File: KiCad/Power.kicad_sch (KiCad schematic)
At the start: 17 parts

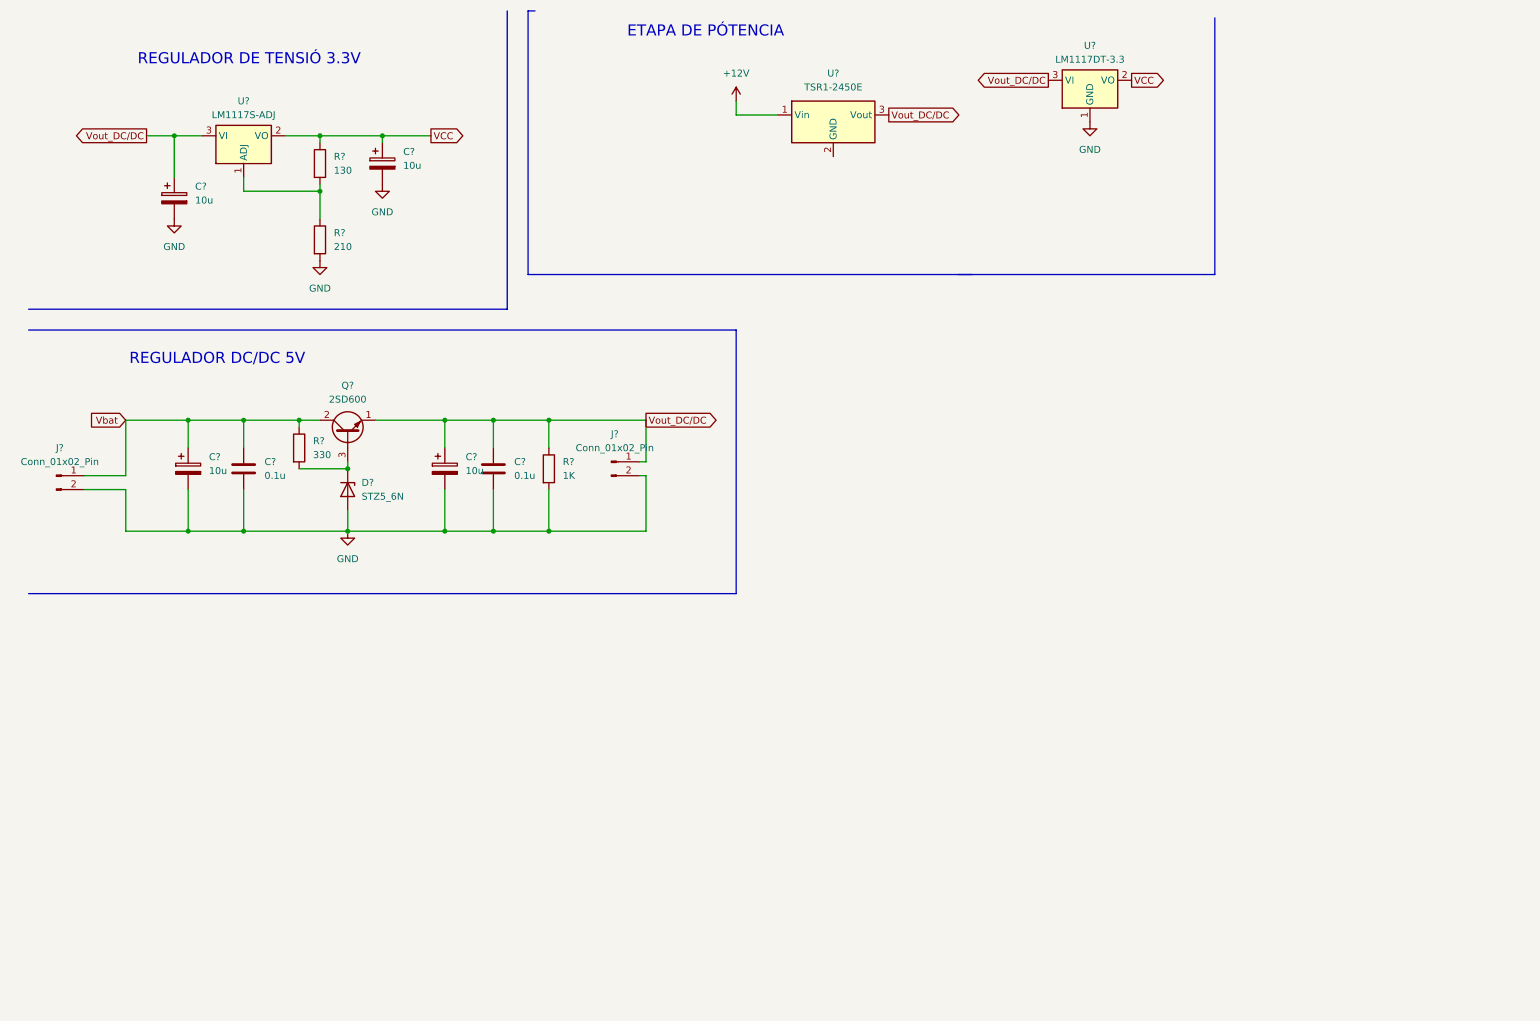
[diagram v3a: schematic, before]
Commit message: Actualización ESquematico arreglandolo y corrigiendo fallos
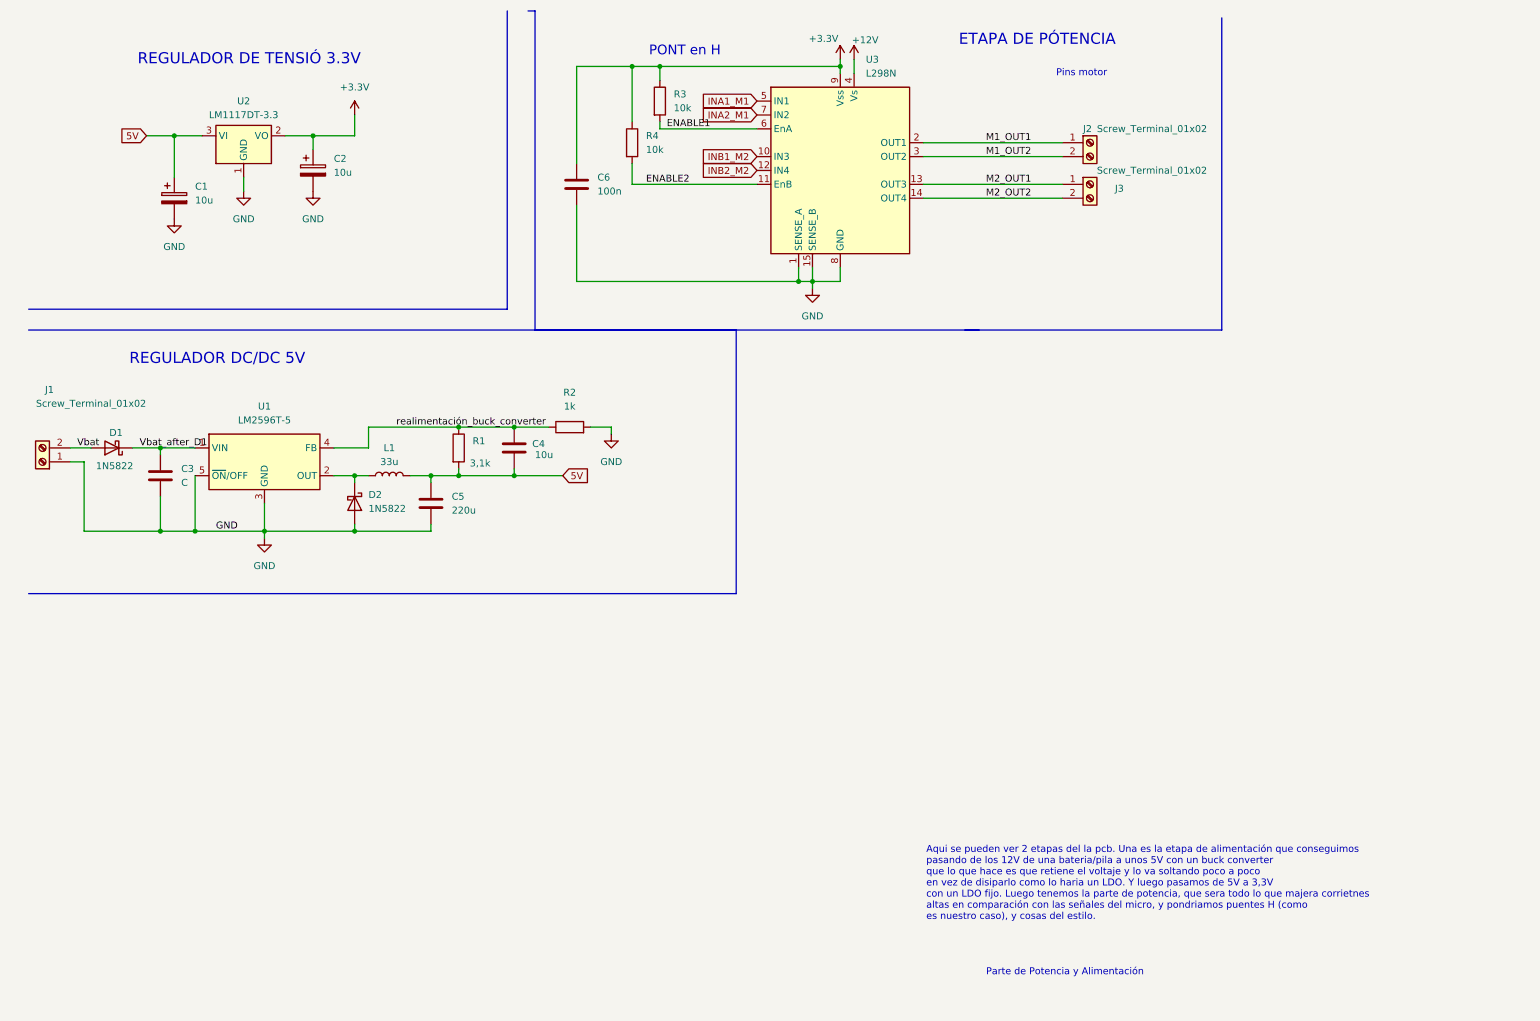
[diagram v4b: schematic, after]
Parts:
- removed C? (x2): 10u, symbol Device:C_Polarized
- removed C? (x2): 0.1u, symbol Device:C
- removed D?: STZ5_6N, symbol Device:D_Zener
- removed J? (x2): Conn_01x02_Pin, symbol Connector:Conn_01x02_Pin
- removed Q?: 2SD600, Package_TO_SOT_THT:TO-126-3_Vertical, symbol Transistor_BJT:2SD600
- removed R?: 1K, symbol Device:R
- removed R?: 210, symbol Device:R
- removed R?: 130, symbol Device:R
- removed R?: 330, symbol Device:R
- removed U?: LM1117DT-3.3, Package_TO_SOT_SMD:TO-252-3_TabPin2, symbol Regulator_Linear:LM1117DT-3.3
- removed U?: LM1117S-ADJ, Package_TO_SOT_SMD:TO-263-3_TabPin2, symbol Regulator_Linear:LM1117S-ADJ
- removed U?: TSR1-2450E, Converter_DCDC:Converter_DCDC_TRACO_TSR1-xxxxE_THT, symbol Converter_DCDC:TSR1-2450E
- added C3: C, symbol Device:C
- added C4: 10u, symbol Device:C
- added C5: 220u, symbol Device:C
- added C6: 100n, symbol Device:C
- added D1, D2: 1N5822, Diode_THT:D_DO-201AD_P15.24mm_Horizontal, symbol Diode:1N5822
- added J1, J2, J3: Screw_Terminal_01x02, symbol Connector:Screw_Terminal_01x02
- added L1: 33u, symbol Device:L
- added R1: 3,1k, symbol Device:R
- added R2: 1k, symbol Device:R
- added R3, R4: 10k, symbol Device:R
- added U1: LM2596T-5, Package_TO_SOT_THT:TO-220-5_P3.4x3.7mm_StaggerOdd_Lead3.8mm_Vertical, symbol Regulator_Switching:LM2596T-5
- added U2: LM1117DT-3.3, Package_TO_SOT_SMD:TO-252-3_TabPin2, symbol Regulator_Linear:LM1117DT-3.3
- added U3: L298N, Package_TO_SOT_THT:TO-220-15_P2.54x5.08mm_StaggerOdd_Lead4.58mm_Vertical, symbol Driver_Motor:L298N
- gave numbers to parts that had none: 2
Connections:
- net +12V: now also U3.4 (Vs)
- net GND: now also C3.2, C5.2, C6.2, D2.2 (A), J1.1 (Pin_1), R2.2, U1.3 (GND), U1.5 (~{ON}/OFF), U2.1 (GND), U3.1 (SENSE_A), U3.15 (SENSE_B), U3.8 (GND)
- net Vbat: now also D1.2 (A), J1.2 (Pin_2)
- net VCC renamed +3.3V
- net +3.3V: now also C6.1, R3.1, R4.1, U2.2 (VO), U3.9 (Vss)
- net Vout_DC/DC renamed 5V
- net 5V: now also C4.2, C5.1, L1.2, R1.2, U2.3 (VI)
- new net: D2.1 (K), L1.1, U1.2 (OUT)
- new net ENABLE1: R3.2, U3.6 (EnA)
- new net ENABLE2: R4.2, U3.11 (EnB)
- new net INA1_M1: U3.5 (IN1)
- new net INA2_M1: U3.7 (IN2)
- new net INB1_M2: U3.10 (IN3)
- new net INB2_M2: U3.12 (IN4)
- new net M1_OUT1: J2.1 (Pin_1), U3.2 (OUT1)
- new net M1_OUT2: J2.2 (Pin_2), U3.3 (OUT2)
- new net M2_OUT1: J3.1 (Pin_1), U3.13 (OUT3)
- new net M2_OUT2: J3.2 (Pin_2), U3.14 (OUT4)
- new net Vbat_after_D1: C3.1, D1.1 (K), U1.1 (VIN)
- new net realimentación_buck_converter: C4.1, R1.1, R2.1, U1.4 (FB)
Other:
- note added: "Aqui se pueden ver 2 etapas del la pcb. Una es la etapa de alimentación que conseguimos pasando de los 12V de una bateria/pila a unos 5V con un buck converter que lo que hace es que retiene el voltaje y lo va soltando poco a poco en vez de disiparlo como lo haria un LDO. Y luego pasamos de 5V a 3,3V con un LDO fijo. Luego tenemos la parte de potencia, que sera todo lo que majera corrietnes altas 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"
- note added: "PONT en H"
- note added: "Parte de Potencia y Alimentación"
- note added: "Pins motor"
- moved on the sheet: C2

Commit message: Nuevos cambios esquemativo v3
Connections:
- net GND: no longer U3.1 (SENSE_A), U3.15 (SENSE_B)
- new net SENSE_A: U3.1 (SENSE_A)
- new net SENSE_B: U3.15 (SENSE_B)
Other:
- note added: "ETAPA DE ALIMENTACIÓ"
- note added: "M1 --> motor del cristal M2 --> motor de la cortineta"
- moved on the sheet: C1, C2, C3, C4, C5, C6, D1, D2, J1, J2, J3, L1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

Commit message: Actualización de Esquematico, he puesto footprints y readme cambiado
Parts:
- C1, C2, C3, C4, C5, C6: footprint (none) -> Capacitor_SMD:C_0805_2012Metric
- J1, J2, J3: footprint (none) -> TerminalBlock:TerminalBlock_MaiXu_MX126-5.0-02P_1x02_P5.00mm
- L1: footprint (none) -> Inductor_SMD:L_1210_3225Metric
- R1, R2, R3, R4: footprint (none) -> Resistor_SMD:R_0805_2012Metric
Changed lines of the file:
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@@
 			)
 		)
-		(property "Footprint" ""
+		(property "Footprint" "Resistor_SMD:R_0805_2012Metric"
 			(at 172.212 100.33 90)
 			(effects
@@
 			)
 		)
-		(property "Footprint" ""
+		(property "Footprint" "TerminalBlock:TerminalBlock_MaiXu_MX126-5.0-02P_1x02_P5.00mm"
 			(at 257.81 107.95 0)
 			(effects
@@
 			)
 		)
-		(property "Footprint" ""
+		(property "Footprint" "Capacitor_SMD:C_0805_2012Metric"
 			(at 115.2652 144.78 0)
 			(effects
@@
 			)
 		)
-		(property "Footprint" ""
+		(property "Footprint" "Capacitor_SMD:C_0805_2012Metric"
 			(at 53.0352 99.06 0)
 			(effects
@@
 			)
 		)
-		(property "Footprint" ""
+		(property "Footprint" "Capacitor_SMD:C_0805_2012Metric"
 			(at 78.4352 93.98 0)
 			(effects
@@
 			)
 		)
-		(property "Footprint" ""
+		(property "Footprint" "Capacitor_SMD:C_0805_2012Metric"
 			(at 50.4952 149.86 0)
 			(effects
@@
 			)
 		)
-		(property "Footprint" ""
+		(property "Footprint" "Capacitor_SMD:C_0805_2012Metric"
 			(at 100.0252 154.94 0)
 			(effects
@@
 			)
 		)
-		(property "Footprint" ""
+		(property "Footprint" "Capacitor_SMD:C_0805_2012Metric"
 			(at 164.7952 111.76 0)
 			(effects
@@
 			)
 		)
-		(property "Footprint" ""
+		(property "Footprint" "Resistor_SMD:R_0805_2012Metric"
 			(at 102.362 140.97 90)
 			(effects
@@
 			)
 		)
-		(property "Footprint" ""
+		(property "Footprint" "TerminalBlock:TerminalBlock_MaiXu_MX126-5.0-02P_1x02_P5.00mm"
 			(at 257.81 100.33 0)
 			(effects
@@
 			)
 		)
-		(property "Footprint" ""
+		(property "Footprint" "Resistor_SMD:R_0805_2012Metric"
 			(at 177.292 92.71 90)
 			(effects
@@
 			)
 		)
-		(property "Footprint" ""
+		(property "Footprint" "Inductor_SMD:L_1210_3225Metric"
 			(at 91.44 146.05 0)
 			(effects
@@
 			)
 		)
-		(property "Footprint" ""
+		(property "Footprint" "Resistor_SMD:R_0805_2012Metric"
 			(at 124.46 138.938 90)
 			(effects
@@
 			)
 		)
-		(property "Footprint" ""
+		(property "Footprint" "TerminalBlock:TerminalBlock_MaiXu_MX126-5.0-02P_1x02_P5.00mm"
 			(at 27.94 143.51 0)
 			(effects

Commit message: Cambios al esquematico por SEsión 3
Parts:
- removed J3: Screw_Terminal_01x02, TerminalBlock:TerminalBlock_MaiXu_MX126-5.0-02P_1x02_P5.00mm, symbol Connector:Screw_Terminal_01x02
- added C35, C36, C37, C38: 100n, Capacitor_SMD:C_0402_1005Metric, symbol Device:C
- added D10, D11, D12, D13, D6, D7, D8, D9: D, Diode_SMD:D_SMC, symbol Device:D
- added J9: Screw_Terminal_01x02, TerminalBlock:TerminalBlock_MaiXu_MX126-5.0-02P_1x02_P5.00mm, symbol Connector:Screw_Terminal_01x02
- renumbered C3 to C13, C1 to C14, C2 to C15, C5 to C16, C4 to C17, C6 to C18, D1 to D3, D2 to D4, J1 to J7, J2 to J8, R2 to R10, R4 to R11, R3 to R12, R1 to R9, U2 to U5, U1 to U6, U3 to U7
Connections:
- net +12V is gone; now on net Vbat: U7.4 (Vs)
- net GND: now also C35.2, C36.2, C37.2, C38.2, D10.2 (A), D13.2 (A), D7.2 (A), D8.2 (A)
- net M1_OUT1: now also J8.2 (Pin_2), C36.1, D6.2 (A), D7.1 (K); no longer J8.1 (Pin_1)
- net M1_OUT2: now also J8.1 (Pin_1), C35.1, D8.1 (K), D9.2 (A); no longer J8.2 (Pin_2)
- net M2_OUT1: now also C37.1, D10.1 (K), D11.2 (A), J9.2 (Pin_2)
- net M2_OUT2: now also C38.1, D12.2 (A), D13.1 (K), J9.1 (Pin_1)
- net Vbat: now also D11.1 (K), D12.1 (K), D6.1 (K), D9.1 (K)
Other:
- moved on the sheet: C18, J8, R11, R12, U7

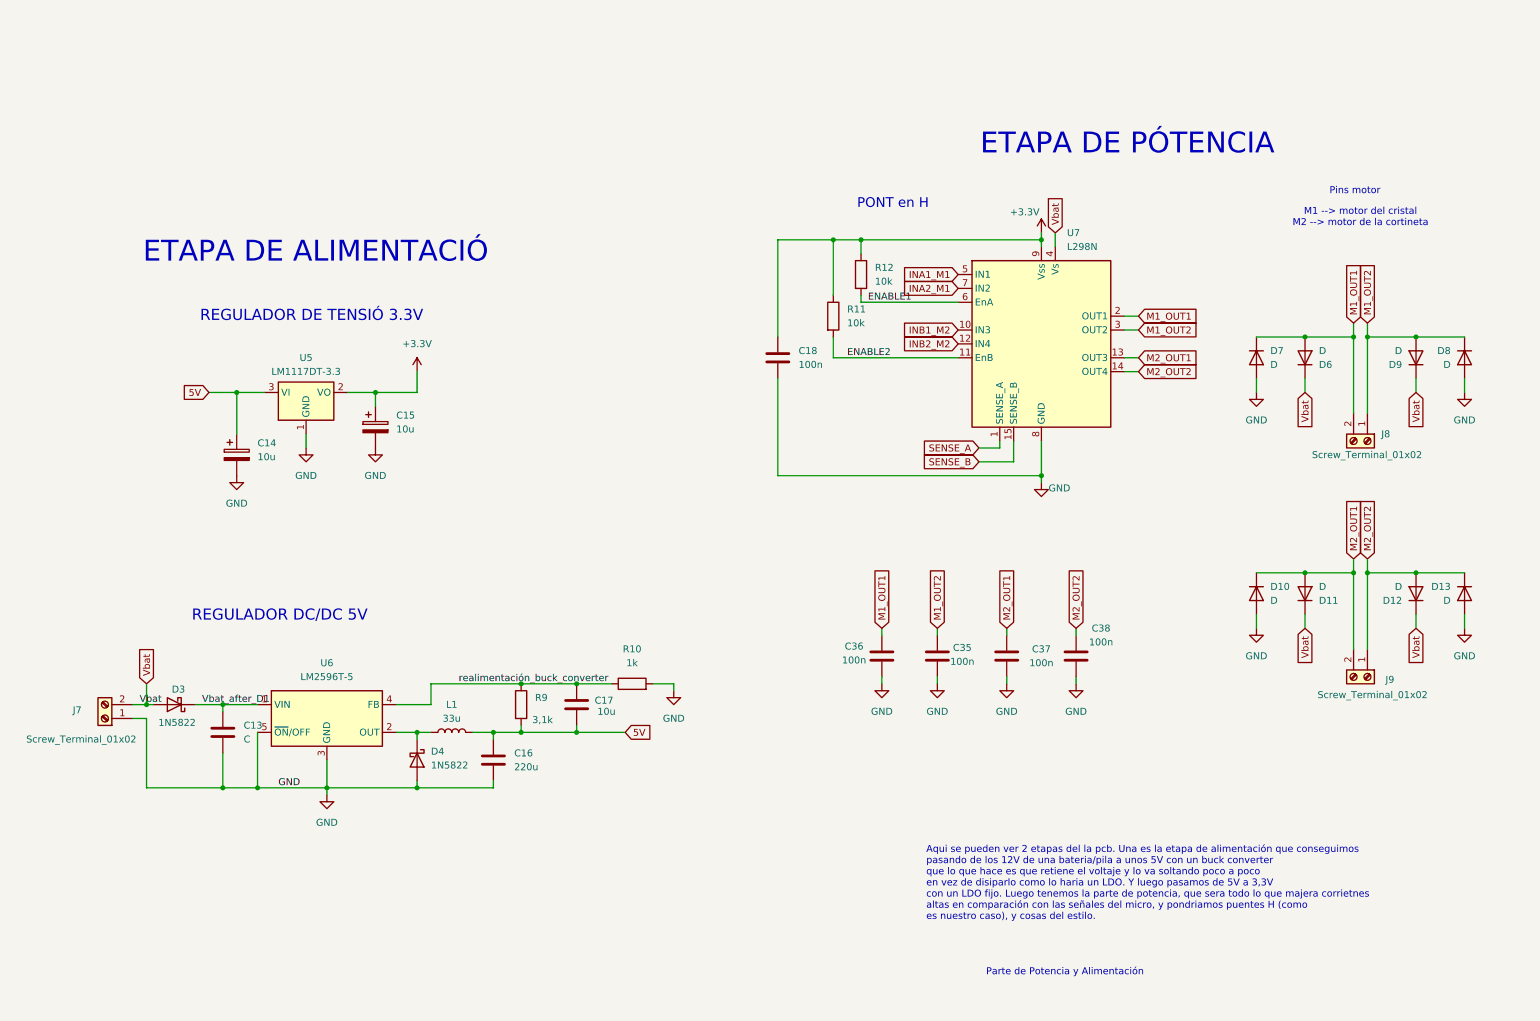
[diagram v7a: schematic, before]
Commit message: pujo el esquematico a medio hacer despues de hacer cambios para mejorar el 2o layout
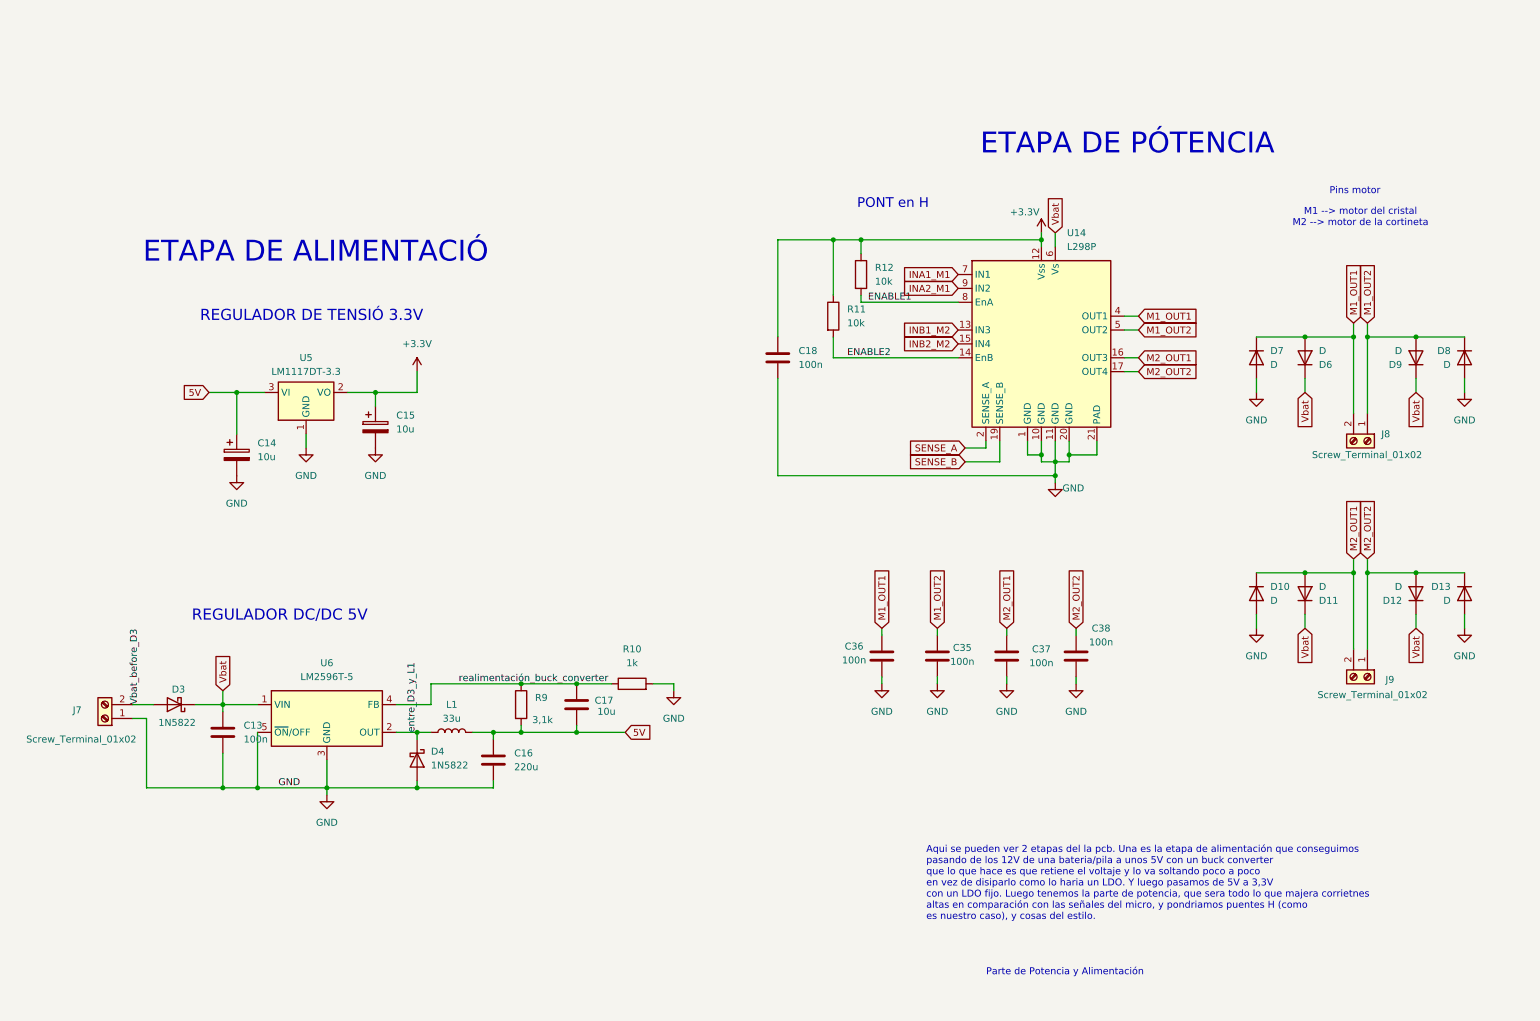
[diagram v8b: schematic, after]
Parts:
- removed U7: L298N, Package_TO_SOT_THT:TO-220-15_P2.54x5.08mm_StaggerOdd_Lead4.58mm_Vertical, symbol Driver_Motor:L298N
- added U14: L298P, Package_SO:HSOP-20-1EP_11.0x15.9mm_P1.27mm_SlugDown_ThermalVias, symbol Driver_Motor:L298P
- C13: value C -> 100n
- C35, C36, C37, C38: footprint Capacitor_SMD:C_0402_1005Metric -> Capacitor_SMD:C_0805_2012Metric
- D10, D11, D12, D13, D6, D7, D8, D9: footprint Diode_SMD:D_SMC -> Diode_SMD:D_SMA
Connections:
- net Vbat_after_D1 is gone; now on net Vbat: C13.1, D3.1 (K), U6.1 (VIN)
- net +3.3V: now also U14.12 (Vss)
- net ENABLE1: now also U14.8 (EnA)
- net ENABLE2: now also U14.14 (EnB)
- net GND: now also U14.1 (GND), U14.10 (GND), U14.11 (GND), U14.20 (GND), U14.21 (PAD)
- net INA1_M1: now also U14.7 (IN1)
- net INA2_M1: now also U14.9 (IN2)
- net INB1_M2: now also U14.13 (IN3)
- net INB2_M2: now also U14.15 (IN4)
- net M1_OUT1: now also U14.4 (OUT1)
- net M1_OUT2: now also U14.5 (OUT2)
- net M2_OUT1: now also U14.16 (OUT3)
- net M2_OUT2: now also U14.17 (OUT4)
- net SENSE_A: now also U14.2 (SENSE_A)
- net SENSE_B: now also U14.19 (SENSE_B)
- net Vbat: now also U14.6 (Vs); no longer D3.2 (A), J7.2 (Pin_2)
- net entre_D3_y_L1: now reaches D4.1 (K), L1.1, U6.2 (OUT)
- new net Vbat_before_D3: D3.2 (A), J7.2 (Pin_2)
